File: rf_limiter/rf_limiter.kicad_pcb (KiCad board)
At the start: 2 copper layers, 22 parts, among them J1 Conn_Coaxial, J2 Conn_Coaxial

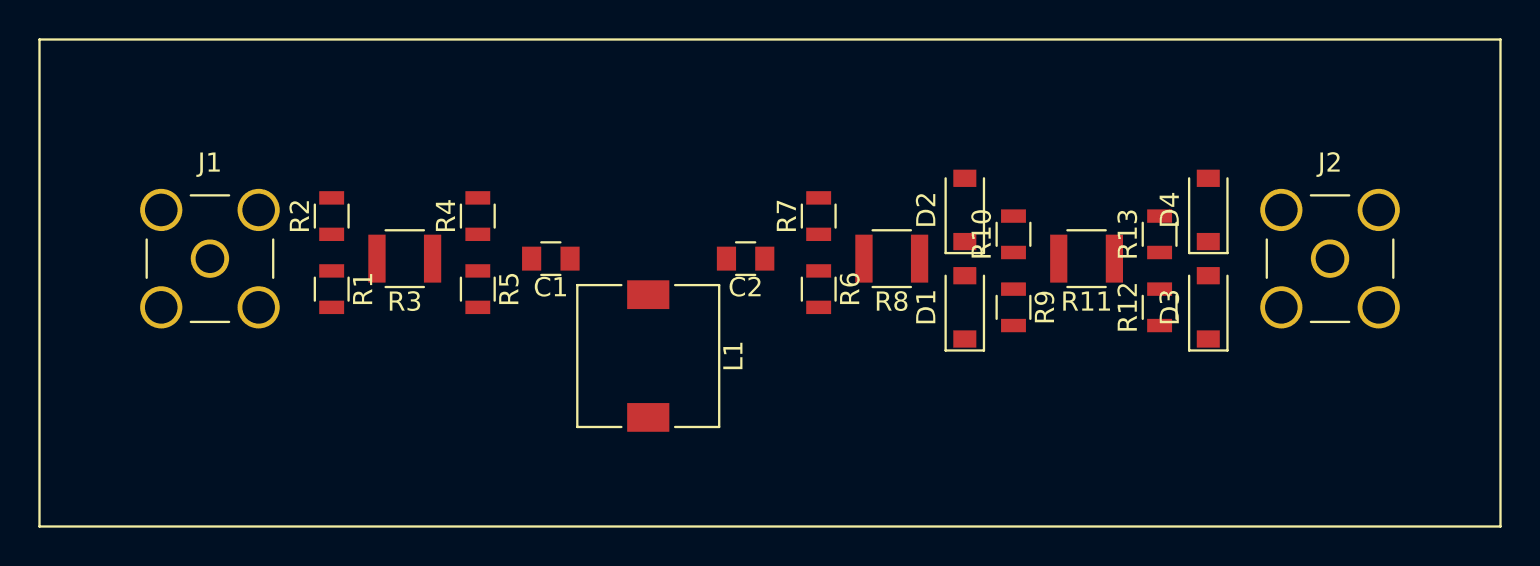
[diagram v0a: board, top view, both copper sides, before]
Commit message: Committed some layout changes. Still need to work out RF stuff. Layout tool is a bit strange when it comes to snapping. Target to fit within 50x50mm PCB
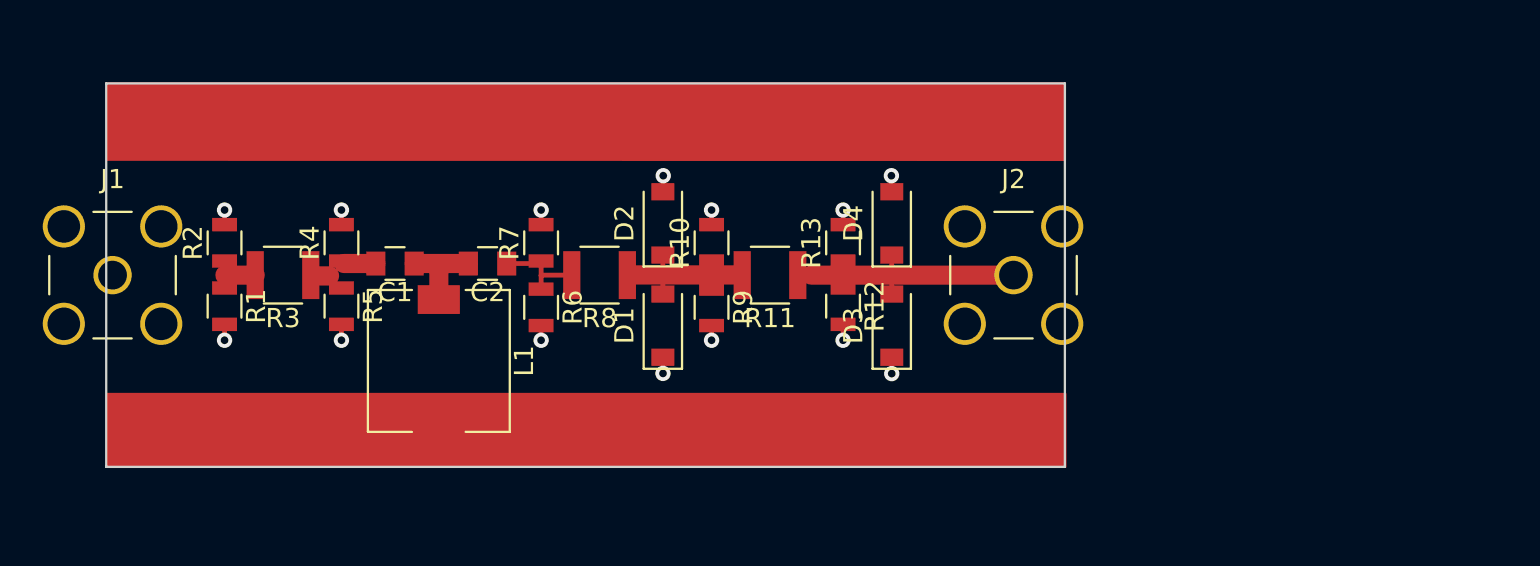
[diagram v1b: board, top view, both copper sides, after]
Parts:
- moved D3 16.5 mm to (141.0, 107.6)
- moved J2 16.5 mm to (147.3, 105.0)
- moved R11 16.5 mm to (134.6, 105.0)
- moved D4 16.5 mm to (141.0, 102.3)
- moved R13 16.5 mm to (138.4, 103.3)
- moved R12 16.5 mm to (138.4, 106.6), turned to 270 degrees
- moved D1 15.8 mm to (129.0, 107.6)
- moved D2 15.8 mm to (129.0, 102.3)
- moved R10 15.8 mm to (131.6, 103.3)
- moved R9 15.7 mm to (131.6, 106.7)
- moved R8 15.3 mm to (125.7, 105.0)
- moved R7 14.5 mm to (122.7, 103.3)
- moved R6 14.5 mm to (122.7, 106.7)
- moved C2 13.5 mm to (119.9, 104.4)
- moved L1 10.9 mm to (117.3, 109.5)
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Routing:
- net Net-(D3-Pad2): track 0.00 -> 14.0 mm
- net GND: track 0.00 -> 11.6 mm, vias 0 -> 14
- net Net-(D1-Pad2): track 0.00 -> 8.79 mm
- net Net-(C2-Pad1): track 0.00 -> 4.92 mm
- net Net-(C1-Pad1): track 0.00 -> 4.59 mm
- net Net-(C1-Pad2): track 0.00 -> 2.55 mm
- net Net-(J1-Pad1): track 0.00 -> 1.58 mm
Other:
- board outline added: 50 x 20 mm
